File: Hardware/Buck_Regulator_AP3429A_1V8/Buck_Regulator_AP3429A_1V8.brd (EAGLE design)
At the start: 25.4 x 25.4 mm, 53 parts, among them J1 Screw Terminal, J2 POWER_JACKPOWER_JACK_SLOT_COM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, J3 Breakout Headers, U1 AP3429/A

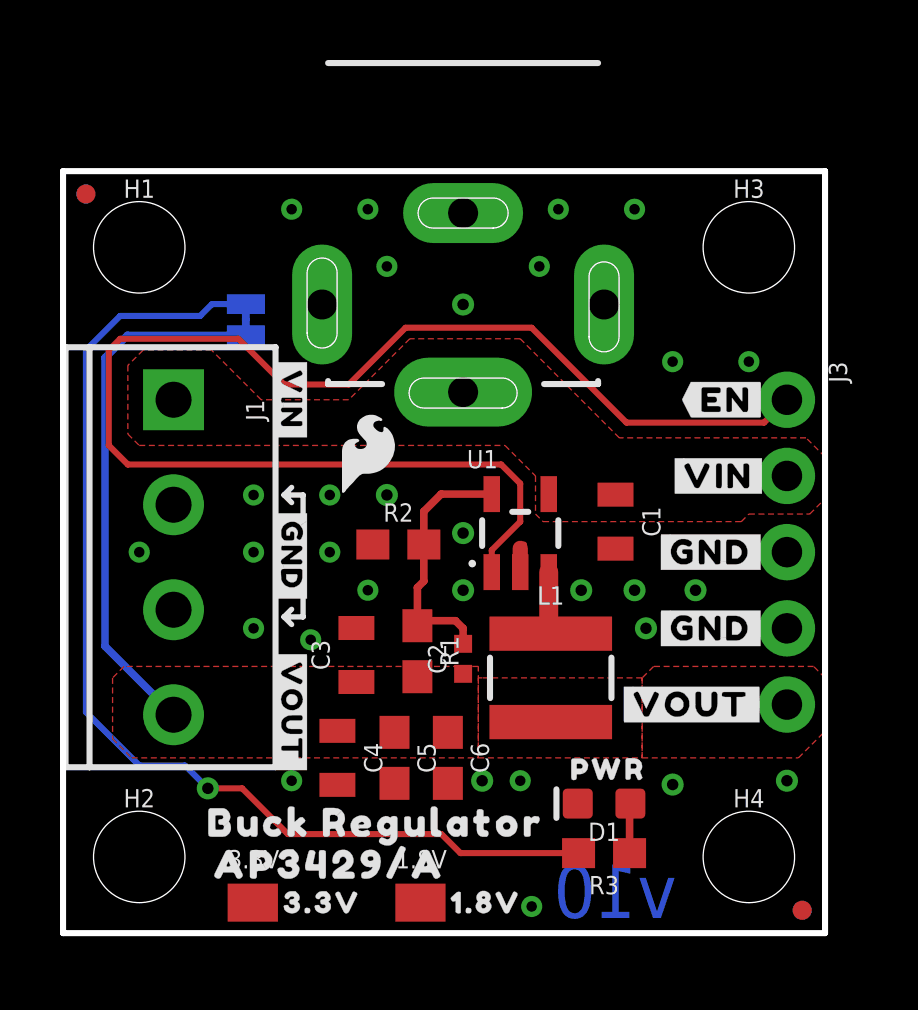
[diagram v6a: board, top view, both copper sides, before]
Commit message: Design Review changes
Cleaned up 1.8V Hardware folder by deleting unneeded files, adjusted schematic notes for easier reading, deleted extraneous measures, adjusted GND via sizes to be the same size (15mil), adjusted some vias for better GND plane connection
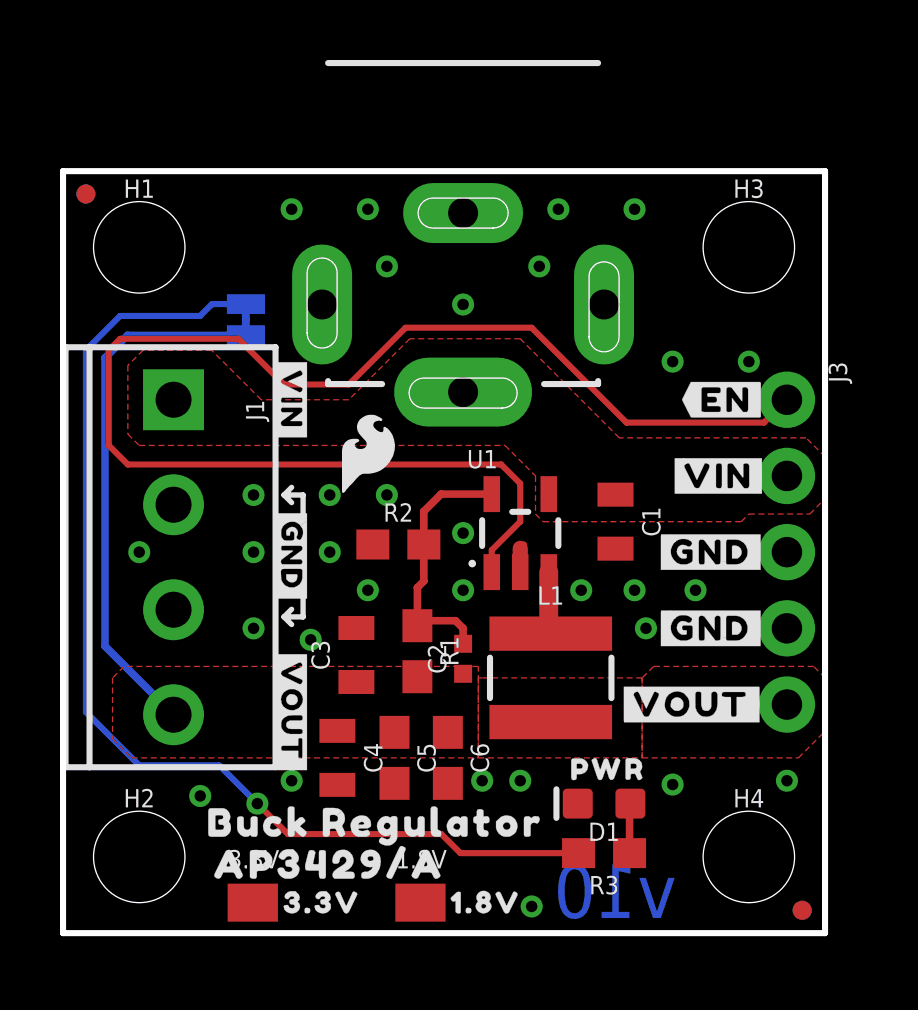
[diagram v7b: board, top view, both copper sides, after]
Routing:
- net GND: vias 30 -> 31
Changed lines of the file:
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@@
 <layer number="28" name="bValues" color="7" fill="1" visible="no" active="yes"/>
 <layer number="29" name="tStop" color="7" fill="3" visible="no" active="yes"/>
-<layer number="30" name="bStop" color="7" fill="6" visible="no" active="yes"/>
+<layer number="30" name="bStop" color="7" fill="6" visible="yes" active="yes"/>
 <layer number="31" name="tCream" color="7" fill="4" visible="no" active="yes"/>
 <layer number="32" name="bCream" color="7" fill="5" visible="no" active="yes"/>
@@
 <layer number="37" name="tTest" color="7" fill="1" visible="no" active="yes"/>
 <layer number="38" name="bTest" color="7" fill="1" visible="no" active="yes"/>
-<layer number="39" name="tKeepout" color="4" fill="11" visible="yes" active="yes"/>
-<layer number="40" name="bKeepout" color="1" fill="11" visible="yes" active="yes"/>
-<layer number="41" name="tRestrict" color="4" fill="10" visible="yes" active="yes"/>
-<layer number="42" name="bRestrict" color="1" fill="10" visible="yes" active="yes"/>
+<layer number="39" name="tKeepout" color="4" fill="11" visible="no" active="yes"/>
+<layer number="40" name="bKeepout" color="1" fill="11" visible="no" active="yes"/>
+<layer number="41" name="tRestrict" color="4" fill="10" visible="no" active="yes"/>
+<layer number="42" name="bRestrict" color="1" fill="10" visible="no" active="yes"/>
 <layer number="43" name="vRestrict" color="2" fill="10" visible="no" active="yes"/>
 <layer number="44" name="Drills" color="7" fill="1" visible="no" active="yes"/>
 <layer number="45" name="Holes" color="7" fill="1" visible="yes" active="yes"/>
 <layer number="46" name="Milling" color="3" fill="1" visible="no" active="yes"/>
-<layer number="47" name="Measures" color="7" fill="1" visible="no" active="yes"/>
+<layer number="47" name="Measures" color="7" fill="1" visible="yes" active="yes"/>
 <layer number="48" name="Document" color="7" fill="1" visible="no" active="yes"/>
 <layer number="49" name="Reference" color="7" fill="1" visible="no" active="yes"/>
@@
 <wire x1="5.08" y1="11.43" x2="5.334" y2="11.176" width="0.2032" layer="22"/>
 <dimension x1="2.54" y1="2.54" x2="0" y2="2.54" x3="1.27" y3="-3.81" textsize="1.778" layer="47" unit="inch"/>
-<dimension x1="3.683" y1="7.28" x2="3.683" y2="0" x3="-3.81" y3="3.64" textsize="1.778" layer="47" dtype="vertical" unit="inch"/>
-<dimension x1="24.13" y1="7.62" x2="24.13" y2="0" x3="-7.62" y3="3.81" textsize="1.778" layer="47" dtype="vertical" unit="inch"/>
-<dimension x1="24.13" y1="10.16" x2="24.13" y2="0" x3="-12.7" y3="5.08" textsize="1.778" layer="47" dtype="vertical" unit="inch"/>
-<dimension x1="3.683" y1="10.795" x2="3.937" y2="0" x3="-17.78" y3="5.3975" textsize="1.778" layer="47" dtype="vertical" unit="inch"/>
 <text x="-22.86" y="-10.16" size="1.778" layer="47" font="vector" ratio="15">Units in Inches</text>
 <dimension x1="3.683" y1="17.78" x2="0" y2="17.78" x3="1.8415" y3="-7.62" textsize="1.778" layer="47" dtype="vertical" unit="inch"/>
 <wire x1="3.048" y1="16.891" x2="3.048" y2="6.35" width="5.9944" layer="48"/>
 <wire x1="3.048" y1="6.35" x2="0" y2="3.302" width="5.9944" layer="48"/>
-<dimension x1="6.35" y1="3.81" x2="0" y2="3.81" x3="3.175" y3="-12.7" textsize="1.778" textratio="15" layer="47" unit="inch"/>
-<dimension x1="13.335" y1="24.003" x2="0" y2="24.003" x3="6.6675" y3="-19.05" textsize="1.778" textratio="15" layer="47" unit="inch"/>
-<dimension x1="22.86" y1="2.54" x2="0" y2="2.54" x3="11.43" y3="-24.13" textsize="1.778" textratio="15" layer="47" unit="inch"/>
-<dimension x1="24.13" y1="7.62" x2="0" y2="7.62" x3="12.065" y3="-29.21" textsize="1.778" textratio="15" layer="47" unit="inch"/>
-<dimension x1="25.4" y1="0" x2="0" y2="0" x3="12.7" y3="-33.02" textsize="1.778" textratio="15" layer="47" unit="inch"/>
-<dimension x1="6.35" y1="3.81" x2="6.35" y2="0" x3="-21.59" y3="1.905" textsize="1.778" textratio="15" layer="47" unit="inch"/>
-<dimension x1="2.54" y1="2.54" x2="2.54" y2="0" x3="-25.4" y3="1.27" textsize="1.778" textratio="15" layer="47" unit="inch"/>
-<dimension x1="2.54" y1="22.86" x2="2.54" y2="0" x3="-29.21" y3="11.43" textsize="1.778" textratio="15" layer="47" unit="inch"/>
-<dimension x1="13.335" y1="24.003" x2="13.335" y2="0" x3="-33.02" y3="12.0015" textsize="1.778" textratio="15" layer="47" unit="inch"/>
-<dimension x1="0" y1="0" x2="0" y2="25.4" x3="-36.83" y3="12.7" textsize="1.778" textratio="15" layer="47" unit="inch"/>
-<dimension x1="6.35" y1="3.81" x2="21.59" y2="3.81" x3="13.97" y3="34.29" textsize="1.778" textratio="15" layer="47" unit="inch"/>
-<dimension x1="21.59" y1="3.81" x2="21.59" y2="16.51" x3="30.48" y3="10.16" textsize="1.778" textratio="15" layer="47" unit="inch"/>
+<dimension x1="3.683" y1="7.28" x2="3.81" y2="0" x3="-2.54" y3="3.64" textsize="1.778" textratio="15" layer="47" dtype="vertical" unit="inch"/>
+<dimension x1="24.13" y1="7.62" x2="24.13" y2="0" x3="-6.35" y3="3.81" textsize="1.778" textratio="15" layer="47" dtype="vertical" unit="inch"/>
+<dimension x1="2.54" y1="2.54" x2="2.54" y2="0" x3="-10.16" y3="1.27" textsize="1.778" textratio="15" layer="47" dtype="vertical" unit="inch"/>
+<dimension x1="0" y1="0" x2="2.54" y2="22.86" x3="-13.97" y3="11.43" textsize="1.778" textratio="15" layer="47" dtype="vertical" unit="inch"/>
+<dimension x1="13.335" y1="24.003" x2="13.97" y2="0" x3="-17.78" y3="12.0015" textsize="1.778" textratio="15" layer="47" dtype="vertical" unit="inch"/>
+<dimension x1="0" y1="0" x2="0" y2="25.4" x3="-21.59" y3="12.7" textsize="1.778" textratio="15" layer="47" unit="inch"/>
+<dimension x1="13.335" y1="24.003" x2="0" y2="24.003" x3="6.6675" y3="-12.7" textsize="1.778" textratio="15" layer="47" unit="inch"/>
+<dimension x1="22.86" y1="2.54" x2="0" y2="2.54" x3="11.43" y3="-17.78" textsize="1.778" textratio="15" layer="47" unit="inch"/>
+<dimension x1="24.13" y1="7.62" x2="0" y2="7.62" x3="12.065" y3="-21.59" textsize="1.778" textratio="15" layer="47" unit="inch"/>
+<dimension x1="0" y1="0" x2="25.4" y2="0" x3="12.7" y3="-26.67" textsize="1.778" textratio="15" layer="47" unit="inch"/>
 </plain>
 <attributes>
@@
 <via x="13.335" y="13.335" extent="1-16" drill="0.381"/>
 <via x="10.795" y="14.605" extent="1-16" drill="0.381"/>
-<via x="8.89" y="14.605" extent="1-16" drill="0.35"/>
-<via x="8.89" y="12.7" extent="1-16" drill="0.35"/>
-<via x="10.16" y="11.43" extent="1-16" drill="0.35"/>
+<via x="8.89" y="14.605" extent="1-16" drill="0.381"/>
+<via x="8.89" y="12.7" extent="1-16" drill="0.381"/>
+<via x="10.16" y="11.43" extent="1-16" drill="0.381"/>
 <via x="17.272" y="11.43" extent="1-16" drill="0.381"/>
-<via x="8.255" y="9.779" extent="1-16" drill="0.35"/>
-<via x="19.05" y="24.13" extent="1-16" drill="0.35"/>
-<via x="7.62" y="24.13" extent="1-16" drill="0.35"/>
-<via x="6.35" y="14.605" extent="1-16" drill="0.35"/>
-<via x="6.35" y="10.16" extent="1-16" drill="0.35"/>
-<via x="15.24" y="5.08" extent="1-16" drill="0.35"/>
-<via x="7.62" y="5.08" extent="1-16" drill="0.35"/>
-<via x="22.86" y="19.05" extent="1-16" drill="0.35"/>
-<via x="20.32" y="19.05" extent="1-16" drill="0.35"/>
-<via x="6.35" y="12.7" extent="1-16" drill="0.35"/>
-<via x="2.54" y="12.7" extent="1-16" drill="0.35"/>
-<via x="15.621" y="0.889" extent="1-16" drill="0.35"/>
-<via x="15.875" y="22.225" extent="1-16" drill="0.35"/>
-<via x="10.795" y="22.225" extent="1-16" drill="0.35"/>
-<via x="16.51" y="24.13" extent="1-16" drill="0.35"/>
-<via x="10.16" y="24.13" extent="1-16" drill="0.35"/>
+<via x="8.255" y="9.779" extent="1-16" drill="0.381"/>
+<via x="19.05" y="24.13" extent="1-16" drill="0.381"/>
+<via x="7.62" y="24.13" extent="1-16" drill="0.381"/>
+<via x="6.35" y="14.605" extent="1-16" drill="0.381"/>
+<via x="6.35" y="10.16" extent="1-16" drill="0.381"/>
+<via x="15.24" y="5.08" extent="1-16" drill="0.381"/>
+<via x="7.62" y="5.08" extent="1-16" drill="0.381"/>
+<via x="22.86" y="19.05" extent="1-16" drill="0.381"/>
+<via x="20.32" y="19.05" extent="1-16" drill="0.381"/>
+<via x="6.35" y="12.7" extent="1-16" drill="0.381"/>
+<via x="2.54" y="12.7" extent="1-16" drill="0.381"/>
+<via x="15.621" y="0.889" extent="1-16" drill="0.381"/>
+<via x="15.875" y="22.225" extent="1-16" drill="0.381"/>
+<via x="10.795" y="22.225" extent="1-16" drill="0.381"/>
+<via x="16.51" y="24.13" extent="1-16" drill="0.381"/>
+<via x="10.16" y="24.13" extent="1-16" drill="0.381"/>
 <contactref element="J2" pad="GND"/>
 <contactref element="C5" pad="2"/>
 <contactref element="C6" pad="2"/>
 <via x="13.97" y="5.08" extent="1-16" drill="0.381"/>
+<via x="4.572" y="4.572" extent="1-16" drill="0.381"/>
 </signal>
 <signal name="N$1">
@@
 <wire x1="13.247" y1="2.667" x2="12.612" y2="3.302" width="0.2032" layer="1"/>
 <wire x1="12.612" y1="3.302" x2="7.493" y2="3.302" width="0.2032" layer="1"/>
-<via x="4.826" y="4.826" extent="1-16" drill="0.381"/>
-<wire x1="4.826" y1="4.826" x2="5.969" y2="4.826" width="0.2032" layer="1"/>
-<wire x1="5.969" y1="4.826" x2="7.493" y2="3.302" width="0.2032" layer="1"/>
+<via x="6.477" y="4.318" extent="1-16" drill="0.381"/>
+<wire x1="6.477" y1="4.318" x2="7.493" y2="3.302" width="0.2032" layer="1"/>
 <wire x1="0.762" y1="19.431" x2="0.762" y2="7.366" width="0.2032" layer="16"/>
 <wire x1="0.762" y1="7.366" x2="2.54" y2="5.588" width="0.2032" layer="16"/>
-<wire x1="4.064" y1="5.588" x2="4.826" y2="4.826" width="0.2032" layer="16"/>
-<wire x1="4.064" y1="5.588" x2="2.54" y2="5.588" width="0.2032" layer="16"/>
+<wire x1="5.207" y1="5.588" x2="6.477" y2="4.318" width="0.2032" layer="16"/>
+<wire x1="5.207" y1="5.588" x2="2.54" y2="5.588" width="0.2032" layer="16"/>
 </signal>
 <signal name="N$4">

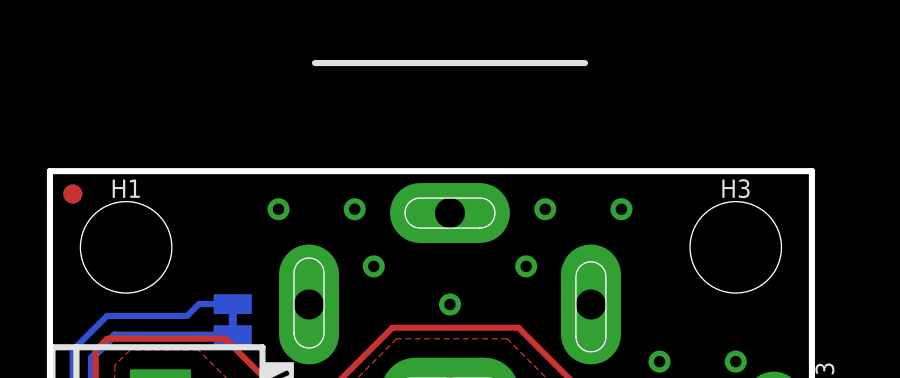
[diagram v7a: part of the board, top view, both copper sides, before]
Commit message: Adjusted power jack for panelizing
There was an issue with overhanging silkscreen for the powerjack since the part is usually populated - the part is not populated for this specific part. This was changed from the device all the way through the panelized files.
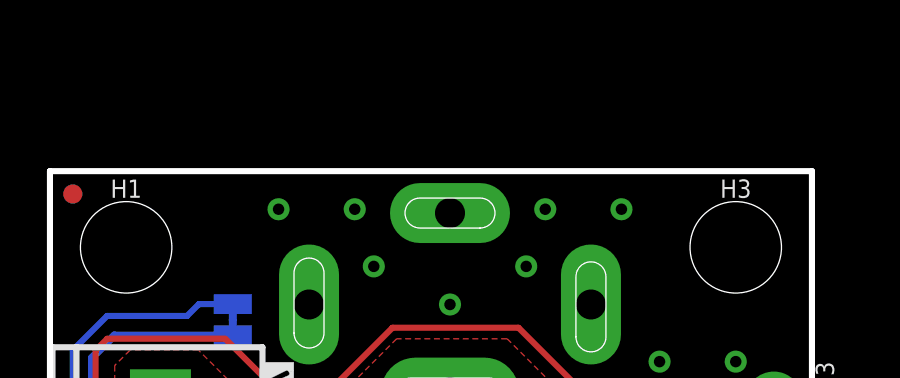
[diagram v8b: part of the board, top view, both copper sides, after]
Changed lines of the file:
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@@
 <drawing>
 <settings>
-<setting alwaysvectorfont="yes"/>
+<setting alwaysvectorfont="no"/>
 <setting verticaltext="up"/>
 </settings>
@@
 <layer number="45" name="Holes" color="7" fill="1" visible="yes" active="yes"/>
 <layer number="46" name="Milling" color="3" fill="1" visible="no" active="yes"/>
-<layer number="47" name="Measures" color="7" fill="1" visible="yes" active="yes"/>
+<layer number="47" name="Measures" color="7" fill="1" visible="no" active="yes"/>
 <layer number="48" name="Document" color="7" fill="1" visible="no" active="yes"/>
 <layer number="49" name="Reference" color="7" fill="1" visible="no" active="yes"/>
@@
 </element>
 <element name="U$16" library="output" package="BUCK_REGULATOR_AP3429#A3453" value="" x="1.524" y="12.827" smashed="yes" rot="MR90"/>
-<element name="J2" library="SparkFun-Connectors" package="POWER_JACK_PTH_SLOT_BOTH" value="POWER_JACKPOWER_JACK_SLOT_COMBO" x="13.335" y="24.003" smashed="yes" rot="R90"/>
 <element name="C5" library="SparkFun-Capacitors" package="0603" value="0.1uF" x="11.049" y="5.842" smashed="yes" rot="R270">
 <attribute name="NAME" x="11.811" y="5.842" size="0.6096" layer="25" font="vector" ratio="20" rot="R270" align="bottom-center"/>
@@
 <attribute name="VALUE" x="12.065" y="5.842" size="0.6096" layer="27" font="vector" ratio="20" rot="R270" align="top-center"/>
 </element>
+<element name="J2" library="SparkFun-Connectors" package="POWER_JACK_PTH_SLOT_BOTH" value="POWER_JACKPOWER_JACK_SLOT_COMBO" x="13.335" y="24.003" smashed="yes" rot="R90"/>
 </elements>
 <signals>
@@
 <via x="16.51" y="24.13" extent="1-16" drill="0.381"/>
 <via x="10.16" y="24.13" extent="1-16" drill="0.381"/>
-<contactref element="J2" pad="GND"/>
 <contactref element="C5" pad="2"/>
 <contactref element="C6" pad="2"/>
 <via x="13.97" y="5.08" extent="1-16" drill="0.381"/>
 <via x="4.572" y="4.572" extent="1-16" drill="0.381"/>
+<contactref element="J2" pad="GND"/>
 </signal>
 <signal name="N$1">
